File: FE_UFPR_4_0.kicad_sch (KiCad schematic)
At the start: 0 parts

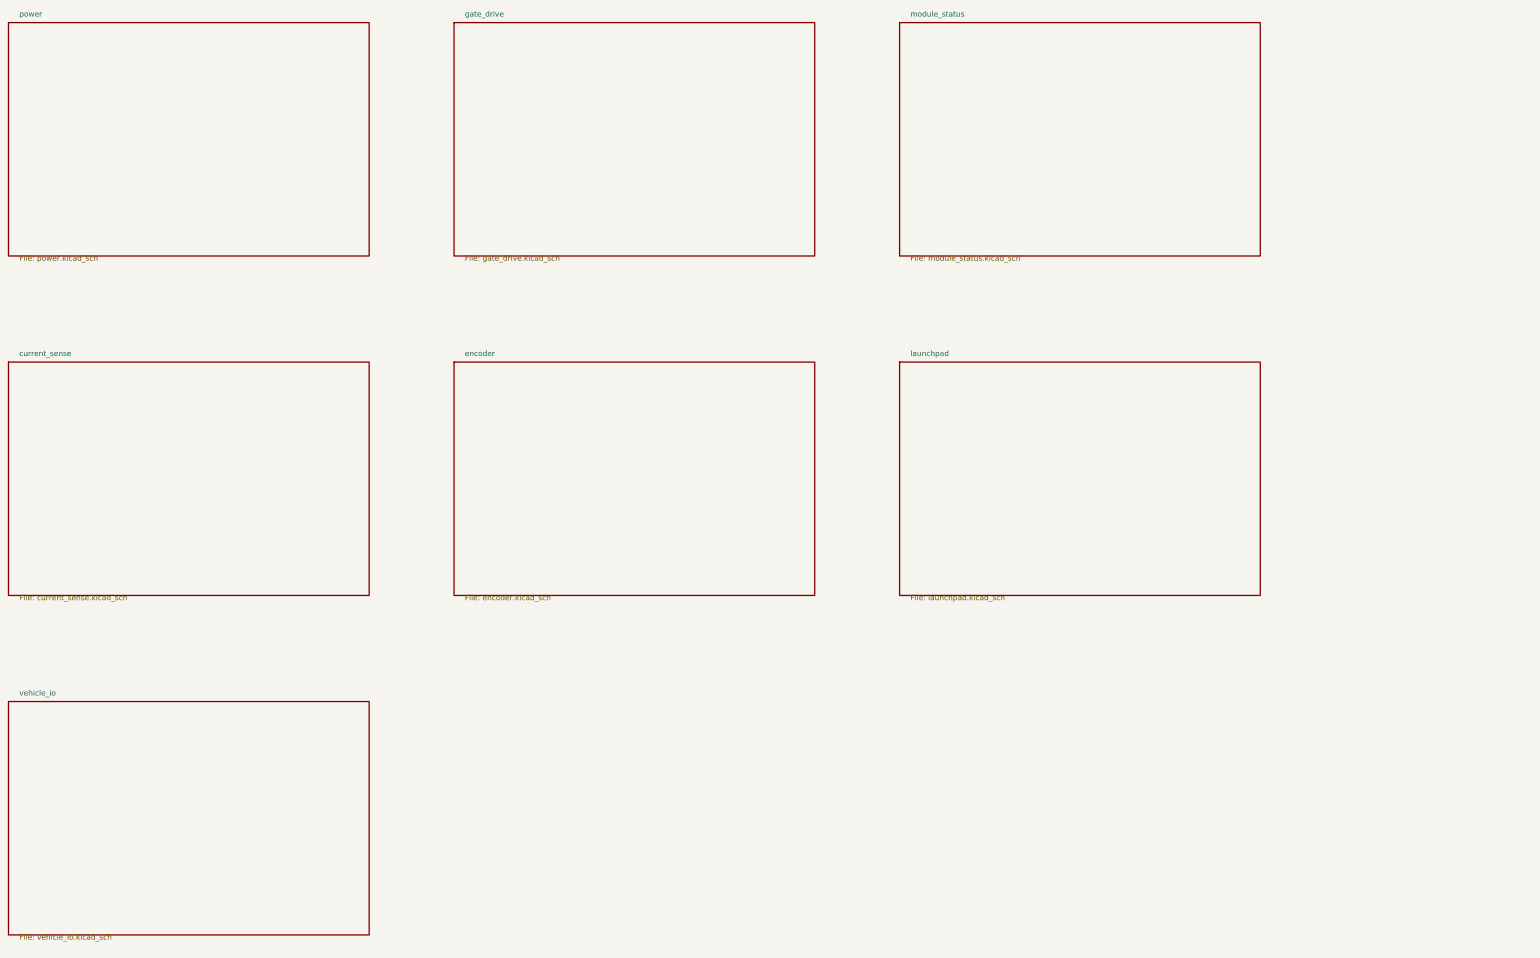
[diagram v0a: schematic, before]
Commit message: S2: system architecture — power tree, grounding, floorplan, root interface
Deliverable: ARCHITECTURE.md (power tree + 3A/49W budget incl. 40W aux
pass-through, LaunchPad power policy JP1/2/3-out JP4/5-in via SPRUI77,
grounding/star/Kelvin + shield tie policy, floorplan inheriting 3.0's
proven DB37/LaunchPad arrangement, adapter-plate mounting plan).

Root sheet: 40 interface nets / 80 sheet pins with stubs + net labels;
matching hierarchical labels pre-declared in all six sub-sheets. Sheet
boxes re-gridded from integer mm to 1.27mm multiples (kills 80 off-grid
warnings). ERC: only the expected 160 label_dangling from the still-empty
hierarchy; zero warnings.

Windfalls: SPRUI77 fetched into datasheets/ — GPIO131 confirmed on header
J6-58, bench items #10/#11 downgraded to verifications. PinSocket_2x10 on
bottom side decided (LaunchPad hangs below). PrimeSTACK drawing is
myInfineon-gated: mounting pattern logged pending user measurement.

Co-Authored-By: Claude Fable 5 <noreply@anthropic.com>
Claude-Session: https://claude.ai/code/session_01QBLb9Rn54VQw2GaKrrnBTE
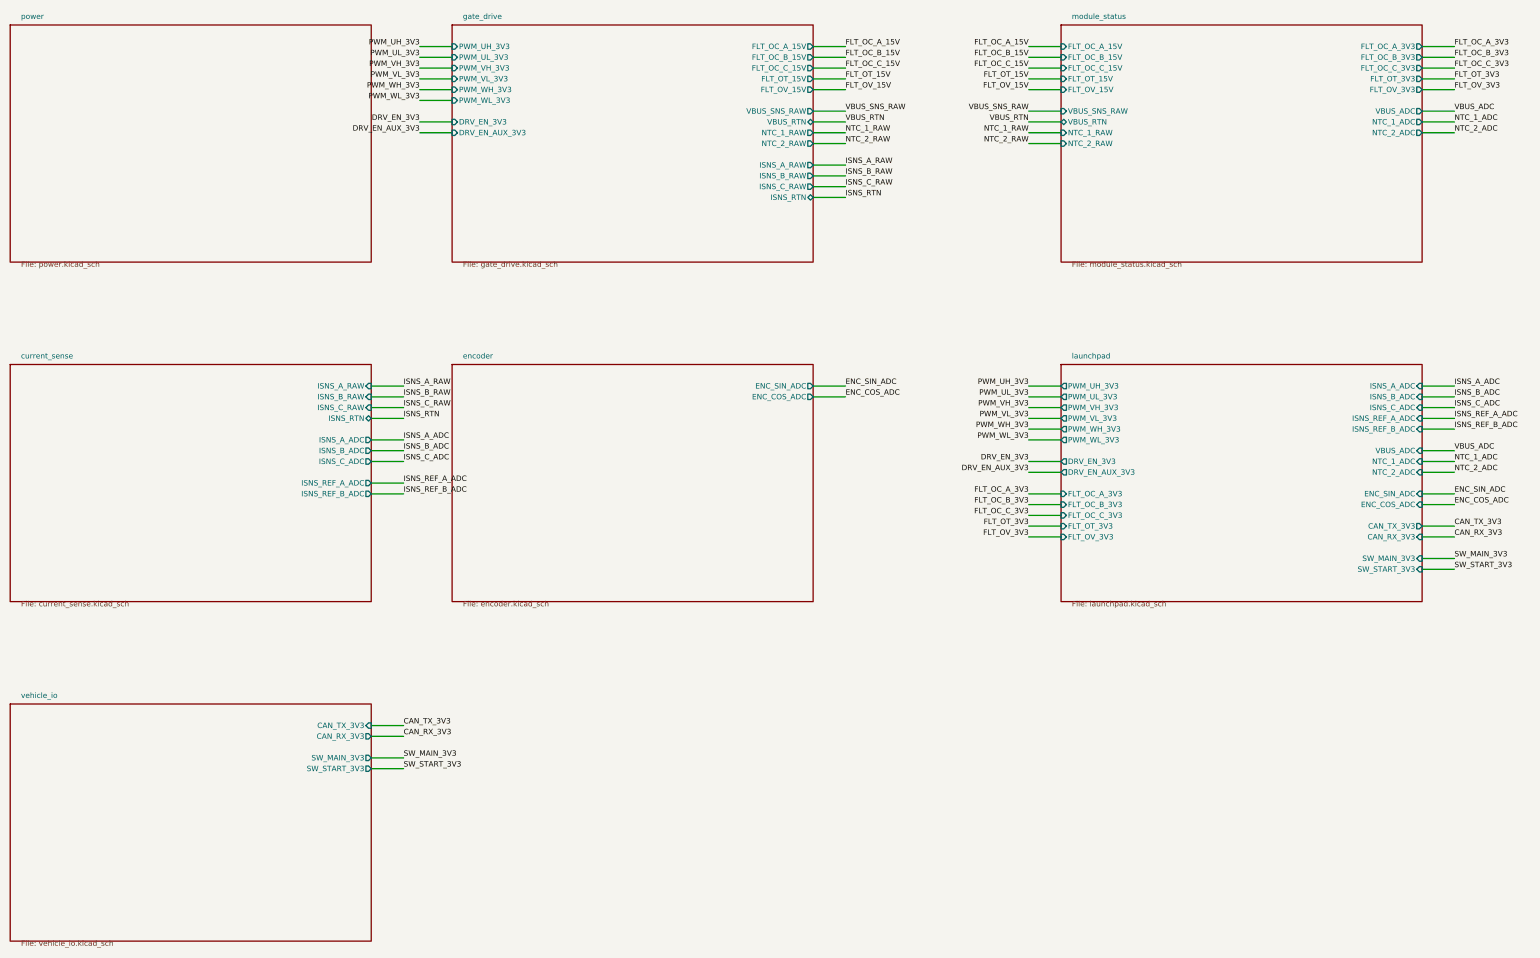
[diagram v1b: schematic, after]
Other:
- sheet current_sense ports: added ISNS_A_ADC, ISNS_A_RAW, ISNS_B_ADC, ISNS_B_RAW, ISNS_C_ADC, ISNS_C_RAW, ISNS_REF_A_ADC, ISNS_REF_B_ADC, ISNS_RTN; removed none
- sheet encoder ports: added ENC_COS_ADC, ENC_SIN_ADC; removed none
- sheet gate_drive ports: added DRV_EN_3V3, DRV_EN_AUX_3V3, FLT_OC_A_15V, FLT_OC_B_15V, FLT_OC_C_15V, FLT_OT_15V, FLT_OV_15V, ISNS_A_RAW, ISNS_B_RAW, ISNS_C_RAW, ISNS_RTN, NTC_1_RAW, NTC_2_RAW, PWM_UH_3V3, PWM_UL_3V3, PWM_VH_3V3, PWM_VL_3V3, PWM_WH_3V3, PWM_WL_3V3, VBUS_RTN, VBUS_SNS_RAW; removed none
- sheet launchpad ports: added CAN_RX_3V3, CAN_TX_3V3, DRV_EN_3V3, DRV_EN_AUX_3V3, ENC_COS_ADC, ENC_SIN_ADC, FLT_OC_A_3V3, FLT_OC_B_3V3, FLT_OC_C_3V3, FLT_OT_3V3, FLT_OV_3V3, ISNS_A_ADC, ISNS_B_ADC, ISNS_C_ADC, ISNS_REF_A_ADC, ISNS_REF_B_ADC, NTC_1_ADC, NTC_2_ADC, PWM_UH_3V3, PWM_UL_3V3, PWM_VH_3V3, PWM_VL_3V3, PWM_WH_3V3, PWM_WL_3V3, SW_MAIN_3V3, SW_START_3V3, VBUS_ADC; removed none
- sheet module_status ports: added FLT_OC_A_15V, FLT_OC_A_3V3, FLT_OC_B_15V, FLT_OC_B_3V3, FLT_OC_C_15V, FLT_OC_C_3V3, FLT_OT_15V, FLT_OT_3V3, FLT_OV_15V, FLT_OV_3V3, NTC_1_ADC, NTC_1_RAW, NTC_2_ADC, NTC_2_RAW, VBUS_ADC, VBUS_RTN, VBUS_SNS_RAW; removed none
- sheet vehicle_io ports: added CAN_RX_3V3, CAN_TX_3V3, SW_MAIN_3V3, SW_START_3V3; removed none

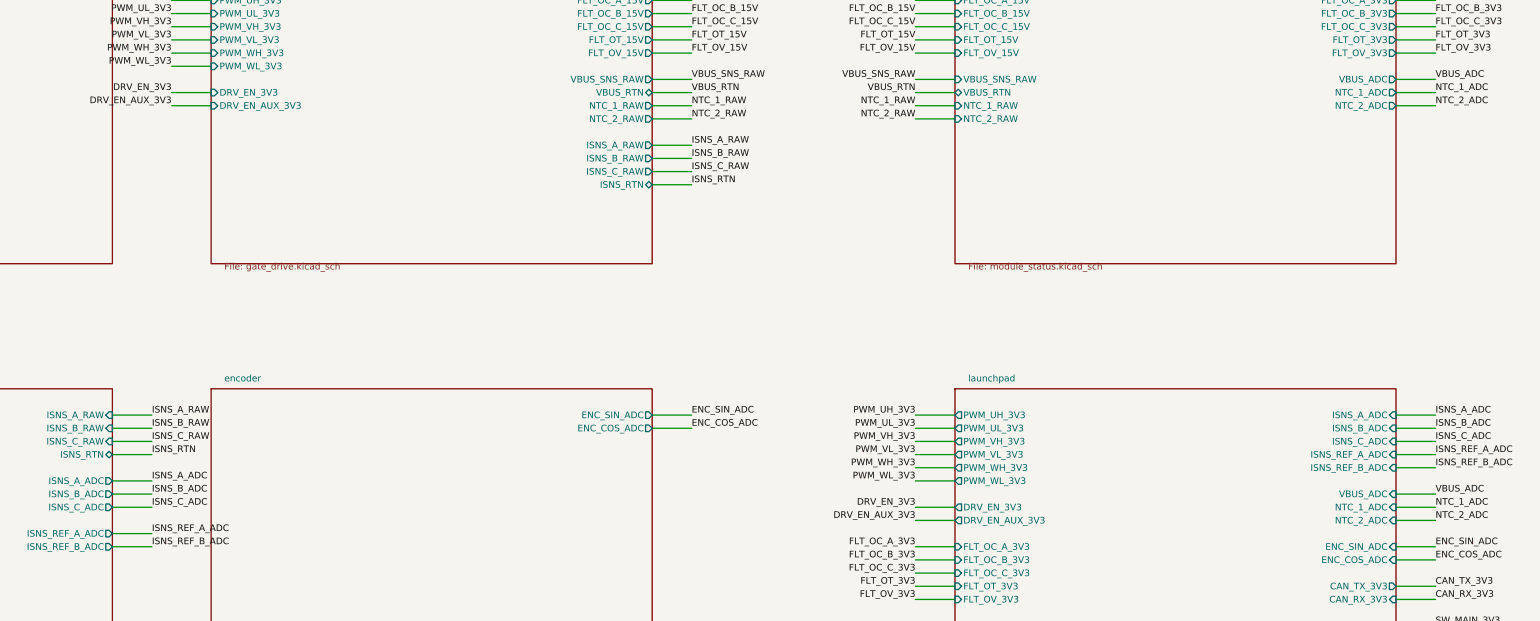
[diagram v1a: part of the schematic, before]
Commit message: S4: gate drive — 3x UCC27524 single stage, hardware enable, DB37 frozen
Replaces 3.0's three-stage chain ('1G126 x6 -> CD4504B -> AND gate powered
from GPIO131) with one stage: 3x UCC27524 dual 5A drivers whose input and
enable thresholds are fixed and independent of VDD, so 3.3V logic switches a
13.5V output stage directly.

The PrimeSTACK datasheet (user-supplied mid-session, now in datasheets/) is
the authoritative source for the DB37 and overturned five inherited beliefs:
  - fault is HIGH, not LOW  -> hw_control_v2.h MODULE_FAULT_ACTIVE_LOW is
    inverted; also makes a disconnected DB37 read as FAULT (fail-safe)
  - analog outputs drive 5 mA -> S5 needs no Vbus buffer op-amp
  - one NTC pin (29), and it is the 10 V channel -> NTC_2_* retired
  - pins 9/27 are a 15V/50mA supply OUTPUT; 3.0 shorted pin 27 to GND
  - pin 1 is true earth/shield, not GND
Bench items #1, #2 and #4 are answered on paper; #5 halves.

Topology chosen on availability first, per the roadmap rule: the whole
TC446x/MIC446x quad family is dead at JLC (TC4468: 14 in stock) against
9550 for the UCC27524.

Safety fix caught during capture: the F28379D powers up with GPIO pull-ups
enabled, so 100k pull-downs would have left the enable and PWM inputs near
2.7V — all six gates armed while the MCU is in reset. Pull-downs are 4.7k.
The enable net's pull-down is 1k because six UCC27524 EN pins present 33k of
internal pull-up to 13.5V.

Numbers: module sees 12.95-13.62 V against an 11-15 V window (validating the
13.5 V rail from S3); worst-case skew 53 ns = 3.5% of the 1500 ns deadband;
effective deadtime 1399 ns; gate path draws ~10 mA.

ARCH CHANGES: NTC_2_RAW/NTC_2_ADC retired; SW_MAIN_3V3 now also feeds
gate_drive as the interlock term; new global net PGND_MOD (DB37 10/28) tied
to GND only at NT2, the 24 V entry star.

gate_drive: 56 components, 44 nets, ERC 0 violations on the sheet, netlist
verified node-by-node (44/44). Libraries 46/46 symbols, 40/40 footprints.
Every part carries an LCSC fiel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
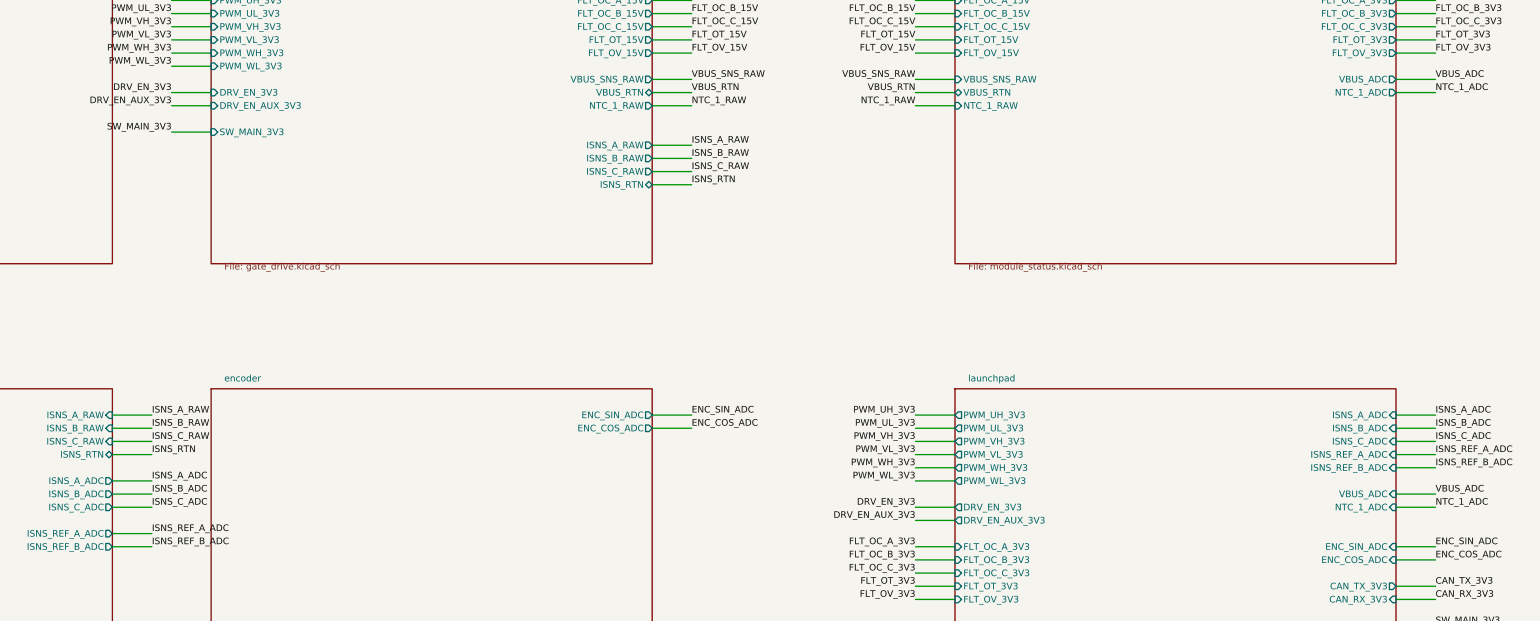
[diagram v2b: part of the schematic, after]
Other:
- sheet gate_drive ports: added SW_MAIN_3V3; removed NTC_2_RAW
- sheet launchpad ports: added none; removed NTC_2_ADC
- sheet module_status ports: added none; removed NTC_2_ADC, NTC_2_RAW
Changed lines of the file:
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@@
+			)
+		)
+		(pin "SW_MAIN_3V3" input
+			(at 129.54 66.04 180)
+			(effects
+				(font
+					(size 1.27 1.27)
+				)
+				(justify left)
 			)
 		)
@@
 		(pin "NTC_1_RAW" output
 			(at 214.63 60.96 0)
-			(effects
-				(font
-					(size 1.27 1.27)
-				)
-				(justify right)
-			)
-		)
-		(pin "NTC_2_RAW" output
-			(at 214.63 63.5 0)
 			(effects
 				(font
@@
 			)
 		)
-		(pin "NTC_2_RAW" input
-			(at 273.05 63.5 180)
-			(effects
-				(font
-					(size 1.27 1.27)
-				)
-				(justify left)
-			)
-		)
 		(pin "FLT_OC_A_3V3" output
 			(at 358.14 40.64 0)
@@
 		(pin "NTC_1_ADC" output
 			(at 358.14 58.42 0)
-			(effects
-				(font
-					(size 1.27 1.27)
-				)
-				(justify right)
-			)
-		)
-		(pin "NTC_2_ADC" output
-			(at 358.14 60.96 0)
 			(effects
 				(font
@@
 			)
 		)
-		(pin "NTC_2_ADC" input
-			(at 358.14 140.97 0)
-			(effects
-				(font
-					(size 1.27 1.27)
-				)
-				(justify right)
-			)
-		)
 		(pin "ENC_SIN_ADC" input
 			(at 358.14 146.05 0)
@@
 	(wire
 		(pts
-			(xy 214.63 63.5) (xy 222.25 63.5)
-		)
-		(stroke
-			(width 0)
-			(type default)
-		)
-	)
-	(label "NTC_2_RAW"
-		(at 222.25 63.5 0)
-		(effects
-			(font
-				(size 1.27 1.27)
-			)
-			(justify left bottom)
-		)
-	)
-	(wire
-		(pts
 			(xy 214.63 68.58) (xy 222.25 68.58)
 		)
@@
 	(wire
 		(pts
-			(xy 273.05 63.5) (xy 265.43 63.5)
-		)
-		(stroke
-			(width 0)
-			(type default)
-		)
-	)
-	(label "NTC_2_RAW"
-		(at 265.43 63.5 180)
-		(effects
-			(font
-				(size 1.27 1.27)
-			)
-			(justify right bottom)
-		)
-	)
-	(wire
-		(pts
 			(xy 358.14 40.64) (xy 365.76 40.64)
 		)
@@
 	(wire
 		(pts
-			(xy 358.14 60.96) (xy 365.76 60.96)
-		)
-		(stroke
-			(width 0)
-			(type default)
-		)
-	)
-	(label "NTC_2_ADC"
-		(at 365.76 60.96 0)
-		(effects
-			(font
-				(size 1.27 1.27)
-			)
-			(justify left bottom)
-		)
-	)
-	(wire
-		(pts
 			(xy 110.49 120.65) (xy 118.11 120.65)
 		)
@@
 	(wire
 		(pts
-			(xy 358.14 140.97) (xy 365.76 140.97)
-		)
-		(stroke
-			(width 0)
-			(type default)
-		)
-	)
-	(label "NTC_2_ADC"
-		(at 365.76 140.97 0)
-		(effects
-			(font
-				(size 1.27 1.27)
-			)
-			(justify left bottom)
-		)
-	)
-	(wire
-		(pts
 			(xy 358.14 146.05) (xy 365.76 146.05)
 		)
@@
 		)
 	)
+	(wire
+		(pts
+			(xy 129.54 66.04) (xy 121.92 66.04)
+		)
+		(stroke
+			(width 0)
+			(type default)
+		)
+	)
+	(label "SW_MAIN_3V3"
+		(at 121.92 66.04 180)
+		(effects
+			(font
+				(size 1.27 1.27)
+			)
+			(justify right bottom)
+		)
+	)
